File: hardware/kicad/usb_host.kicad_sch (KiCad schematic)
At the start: 6 parts, among them J3 USB-A_Host, U7 MAX3421E, Y1 12MHz

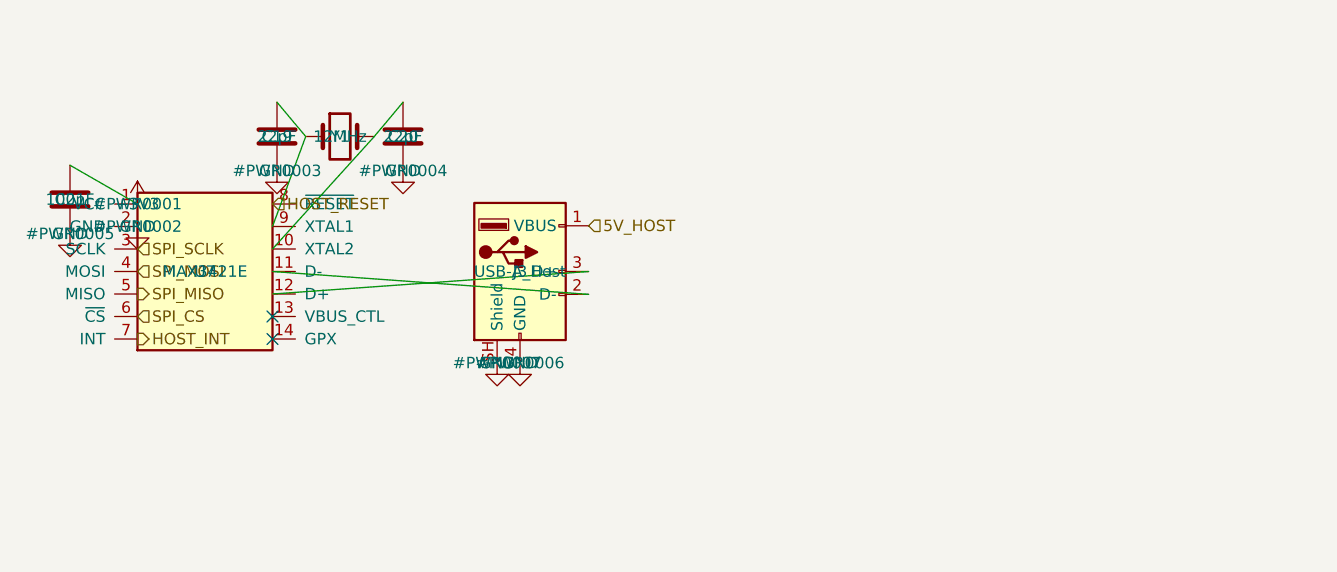
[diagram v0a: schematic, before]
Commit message: fix: repair schematic connectivity, real MAX3421E pinout, footprint assignment
- Root sheet pins were placed outside the sheet boxes, so no cross-sheet
  net (IO5->CI-V, USB D+/D-, SPI, VBUS_5V, 5V_HOST) was actually connected.
  Rebuilt pins on the sheet borders with wire stubs + labels.
- MCU: SW1/SW2 pin 2 carried both GND and EN/BOOT0 (short to ground);
  GND moved to pin 1. Unused ESP32 GPIOs marked no-connect.
- USB_Host rebuilt around the real MAX3421E TQFN-32 pinout (datasheet
  19-3953): 33 ohm D+/D- series resistors, 1uF VCC/VBCOMP, 0.1uF VL.
- J1 now AudioJack3 (T/R/S) with CUI SJ1-3523N footprint; Q1 is a real
  2N7000 (TO-92).
- PWR_FLAGs added; ERC (raw kicad-cli) has 0 errors.
- Board outline 65x45 mm, 54 footprints assigned and written to symbol
  Footprint fields, netlist applied. Placement is a rough grid only; no
  routing yet.
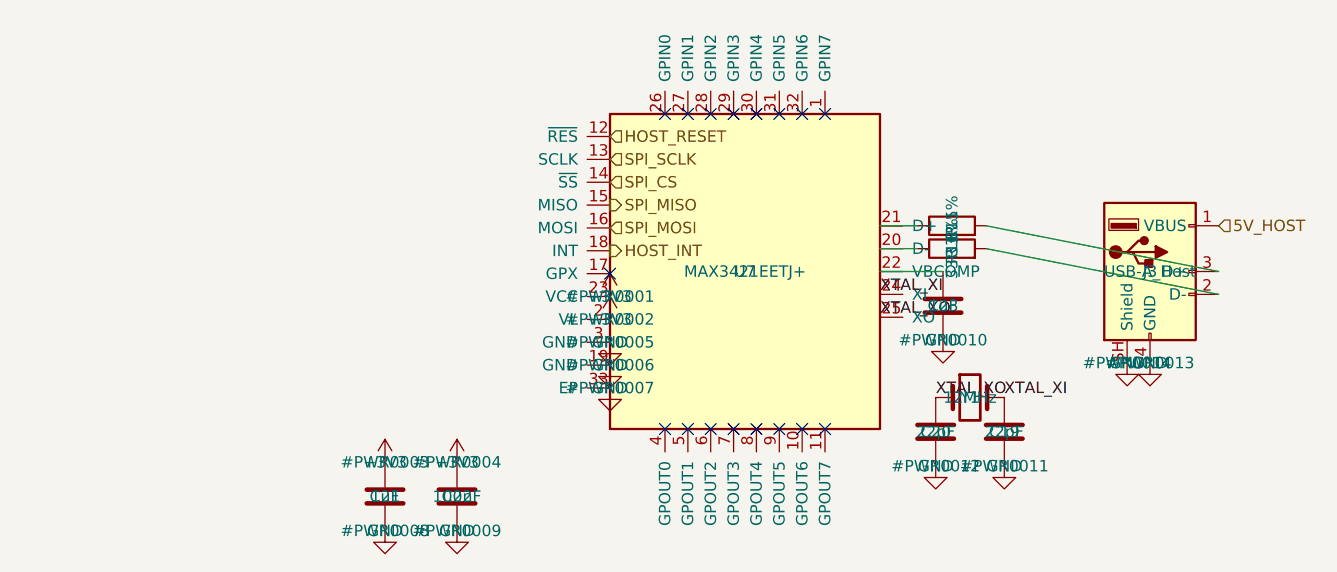
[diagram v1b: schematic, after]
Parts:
- removed U7: MAX3421E, Package_DFN_QFN:QFN-32-1EP_5x5mm_P0.5mm_EP3.7x3.7mm, symbol WaveRig_Custom:MAX3421E
- added C22: 100nF, Capacitor_SMD:C_0603_1608Metric, symbol Device:C
- added C23: 1uF, Capacitor_SMD:C_0603_1608Metric, symbol Device:C
- added R15, R16: 33R 1%, Resistor_SMD:R_0603_1608Metric, symbol Device:R
- added U7: MAX3421EETJ+, Package_DFN_QFN:QFN-32-1EP_5x5mm_P0.5mm_EP3.7x3.7mm, symbol WaveRig_Custom:MAX3421E_TQFN32
- C19, C20: footprint (none) -> Capacitor_SMD:C_0603_1608Metric
- C21: value 100nF -> 1uF; footprint (none) -> Capacitor_SMD:C_0603_1608Metric
- J3: footprint (none) -> Connector_USB:USB_A_Receptacle_GCT_USB1046
- Y1: footprint (none) -> Crystal:Crystal_SMD_HC49-SD
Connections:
- net +3V3: now also C22.1, U7.2 (VL), U7.23 (VCC)
- net GND: now also C22.2, C23.2, U7.19 (GND), U7.3 (GND), U7.33 (EP)
- net HOST_INT: now also U7.18 (INT)
- net HOST_RESET: now also U7.12 (~{RES})
- net SPI_CS: now also U7.14 (~{SS})
- net SPI_MISO: now also U7.15 (MISO)
- net SPI_MOSI: now also U7.16 (MOSI)
- net SPI_SCLK: now also U7.13 (SCLK)
- net XTAL_XI: now reaches Y1.2
- net XTAL_XI: now also C19.1, U7.24 (XI); no longer C20.1
- net at J3.2 (D-): now also R16.2
- net at J3.3 (D+): now also R15.2
- net XTAL_XO: now reaches Y1.1
- net XTAL_XO: now also C20.1, U7.25 (XO); no longer C19.1
- new net: R16.1, U7.20 (D-)
- new net: R15.1, U7.21 (D+)
- new net: C23.1, U7.22 (VBCOMP)
- no-connect marks 2 -> 17

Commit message: docs: specify Y1 crystal parameters (CL18pF, ESR 60R max) per MAX3421E datasheet
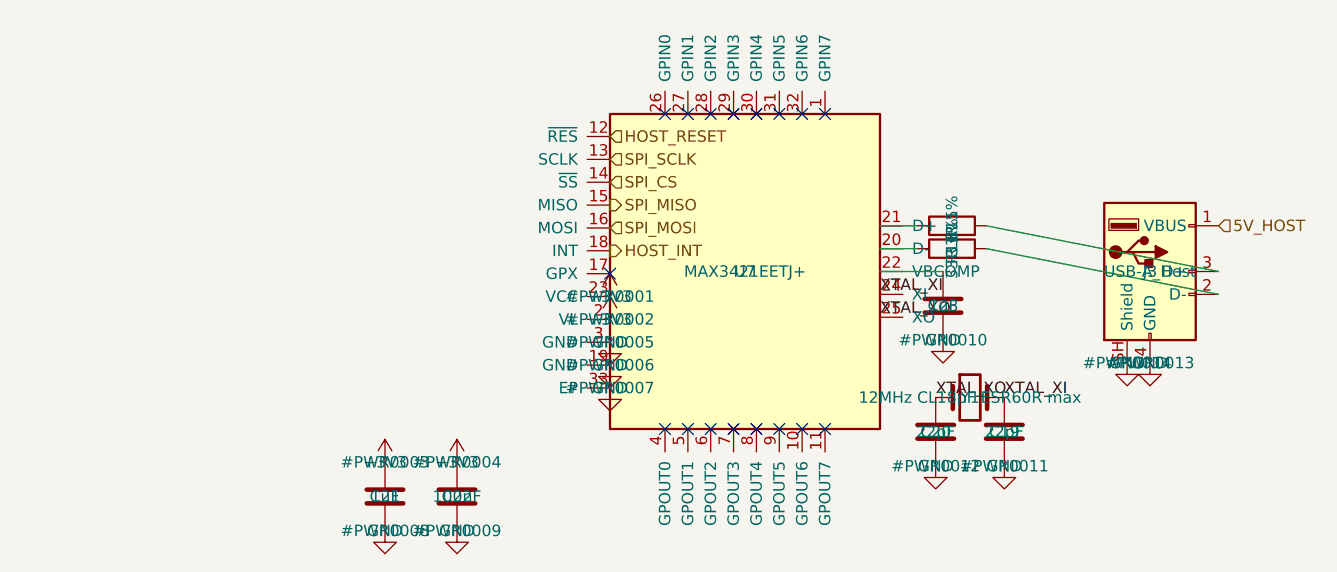
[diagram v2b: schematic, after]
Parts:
- Y1: value 12MHz -> 12MHz CL18pF ESR60R max
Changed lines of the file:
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@@
 			)
 		)
-		(property "Value" "12MHz"
+		(property "Value" "12MHz CL18pF ESR60R max"
 			(at 125 124 0)
 			(effects
